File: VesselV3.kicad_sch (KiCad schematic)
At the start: 376 parts, among them J1 JTAG/SWD 10pins Headers, Q1 BC856A,215, Y1 25MHz

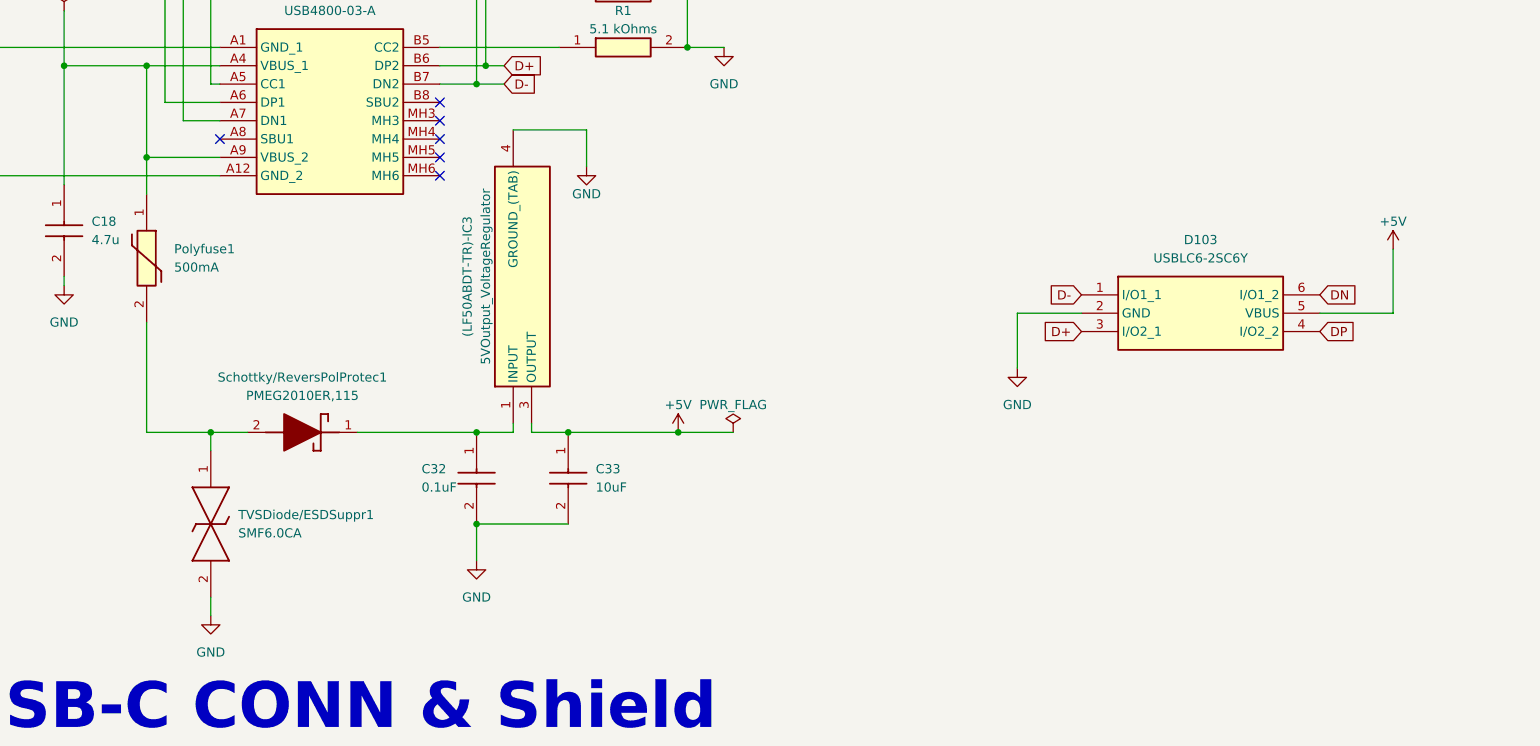
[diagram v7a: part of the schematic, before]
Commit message: New LDO - 1.5 Amps compatibility test start
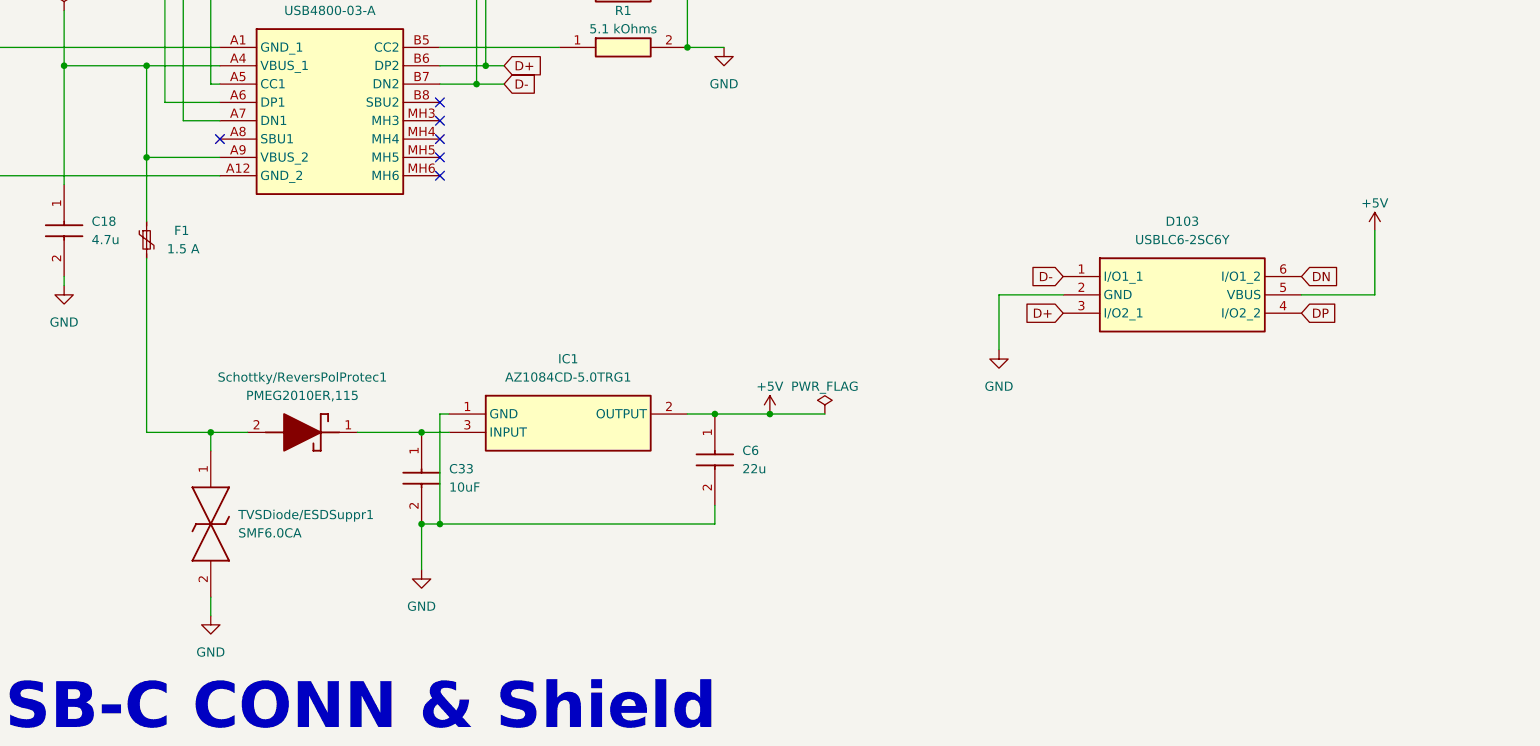
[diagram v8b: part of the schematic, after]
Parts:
- removed (LF50ABDT-TR)-IC3: 5VOutput_VoltageRegulator, SamacSys_Parts:TO228P972X240-3N, symbol SamacSys_Parts:LF50ABDT-TR
- removed C32: 0.1uF, SamacSys_Parts:CAPC1005X55N, symbol SamacSys_Parts:GRM155R71A104JA01D
- removed Polyfuse1: 500mA, SamacSys_Parts:1206L05015YR, symbol SamacSys_Parts:1206L050_15YR
- added C6: 22u, SamacSys_Parts:CAPC2012X75N, symbol SamacSys_Parts:CL21A226MPQNNNE
- added F1: Polyfuse_Small, SamacSys_Parts:FUSC4632X110N, symbol Device:Polyfuse_Small
- added IC1: AZ1084CD-5.0TRG1, SamacSys_Parts:AZ1084CD50TRG1, symbol SamacSys_Parts:AZ1084CD-5.0TRG1
- D103: DigikeyPartNumber (none) -> 497-11882-2-ND
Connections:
- net +5V: now also C6.1, IC1.2 (OUTPUT); no longer C33.1
- net GND: now also C6.2, IC1.1 (GND)
- net at Schottky/ReversPolProtec1.1 (K): now also C33.1, IC1.3 (INPUT)
- net at C18.1, USB-C1.A4 (VBUS_1), USB-C1.A9 (VBUS_2): now also F1.1
- net at Schottky/ReversPolProtec1.2 (A), TVSDiode/ESDSuppr1.1: now also F1.2
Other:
- moved on the sheet: C33, D103
